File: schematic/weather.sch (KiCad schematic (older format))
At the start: 17 parts, among them J1 CONN_01X02, J2 CONN_01X02, J3 CONN_01X04, SW1 SW_SPDT, U1 HT7333A, U2 BME280, U3 TP4056_module, U4 HT7333A, U5 ESP32_adapter_board

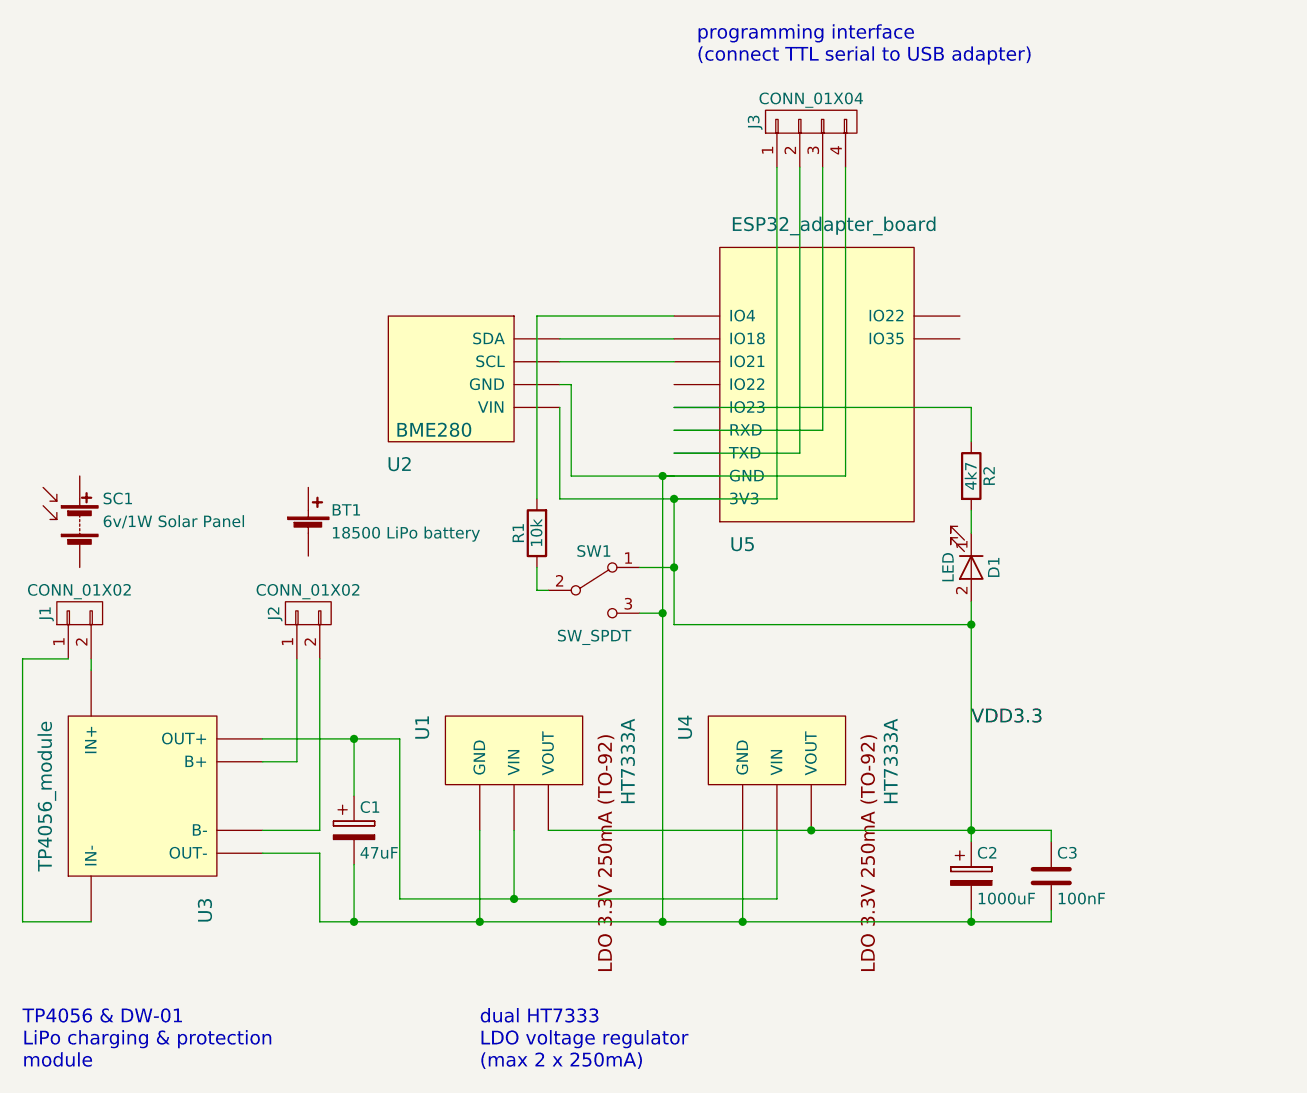
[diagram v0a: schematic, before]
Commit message: added soil sensor schematic
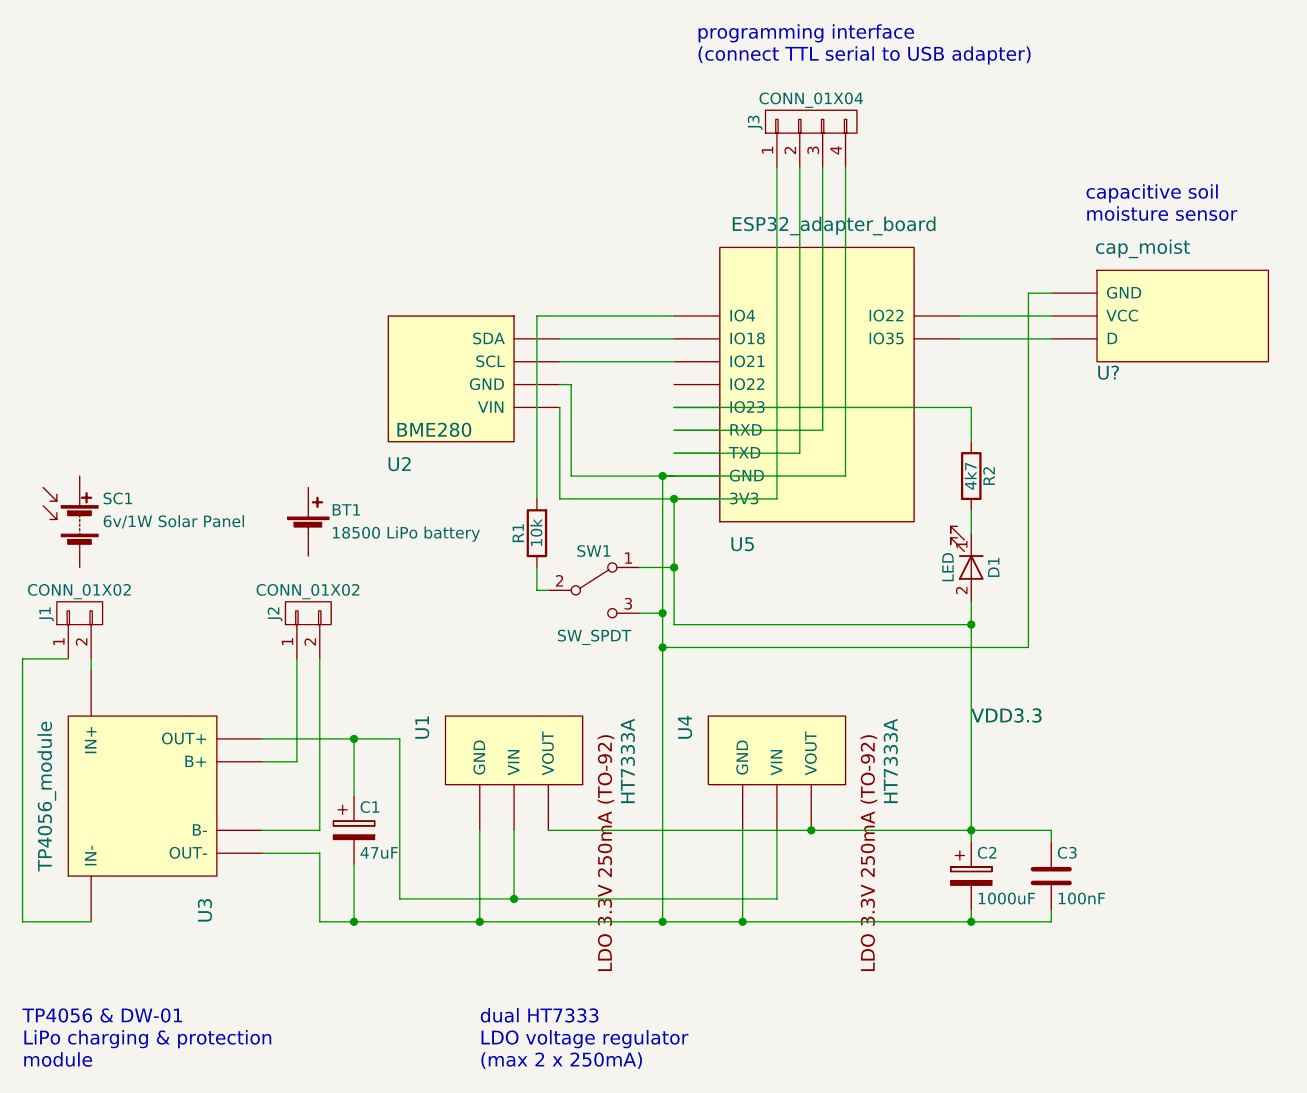
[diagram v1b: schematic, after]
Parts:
- added U?: cap_moist, symbol cap_moist
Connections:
- net at C1.2, C2.2, C3.2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: now also U?.~ (VCC)
- new net: U2.~ (VIN), U5.~ (TXD) (x2)
- new net: U5.~ (TXD), U?.~ (VCC) (x2)
- new net: C1.1, U1.~ (VOUT), U3.~ (OUT-), U4.~ (VOUT)
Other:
- note added: "capacitive soil\nmoisture sensor"
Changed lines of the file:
@@
 LIBS:valves
 LIBS:switches
+LIBS:mylib
 LIBS:weather-cache
 EELAYER 25 0
@@
 Text Notes 6150 1650 0    60   ~ 0
 programming interface\n(connect TTL serial to USB adapter)
+$Comp
+L cap_moist U?
+U 1 1 5B8AD40B
+P 7450 3250
+F 0 "U?" H 7950 3500 60  0000 C CNN
+F 1 "cap_moist" H 8100 4050 60  0000 C CNN
+F 2 "" H 7450 3250 60  0001 C CNN
+F 3 "" H 7450 3250 60  0001 C CNN
+	1    7450 3250
+	1    0    0    -1
+$EndComp
+Wire Wire Line
+	7300 2750 7700 2750
+Wire Wire Line
+	7700 2850 7300 2850
+Connection ~ 6000 4200
+Wire Wire Line
+	7700 2650 7600 2650
+Wire Wire Line
+	7600 2650 7600 4200
+Wire Wire Line
+	7600 4200 6000 4200
+Text Notes 7850 2350 0    60   ~ 0
+capacitive soil\nmoisture sensor
 $EndSCHEMATC
